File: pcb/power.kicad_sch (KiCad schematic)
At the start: 13 parts, among them J5 12V INPUT 5.08mm >=10A, Q1 FQP47P06 reverse-polarity, U4 AP63205WU-7 fixed 5V

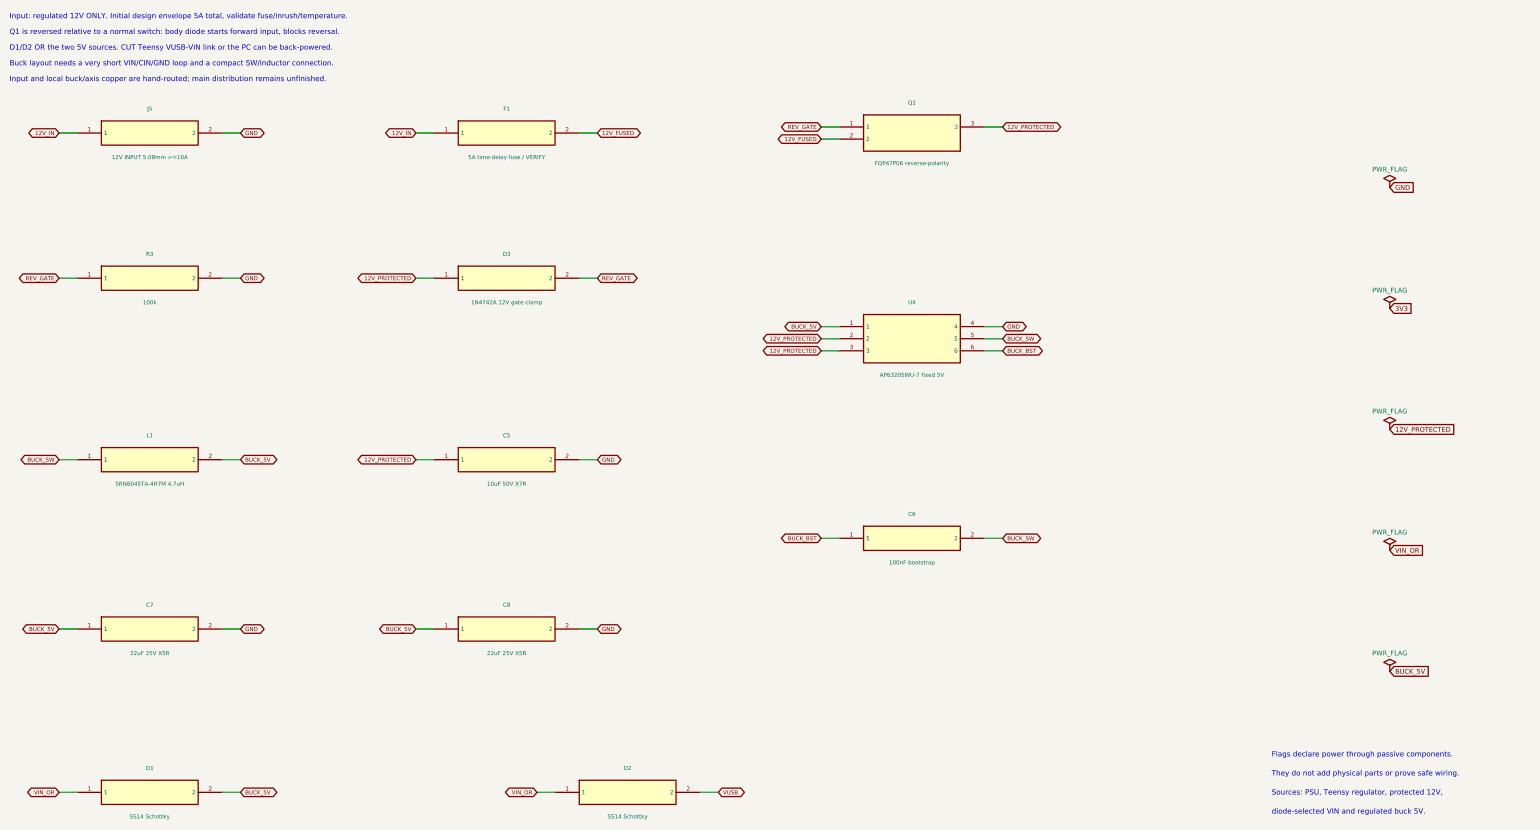
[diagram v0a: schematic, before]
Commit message: feat: finish through-hole six-axis carrier review design
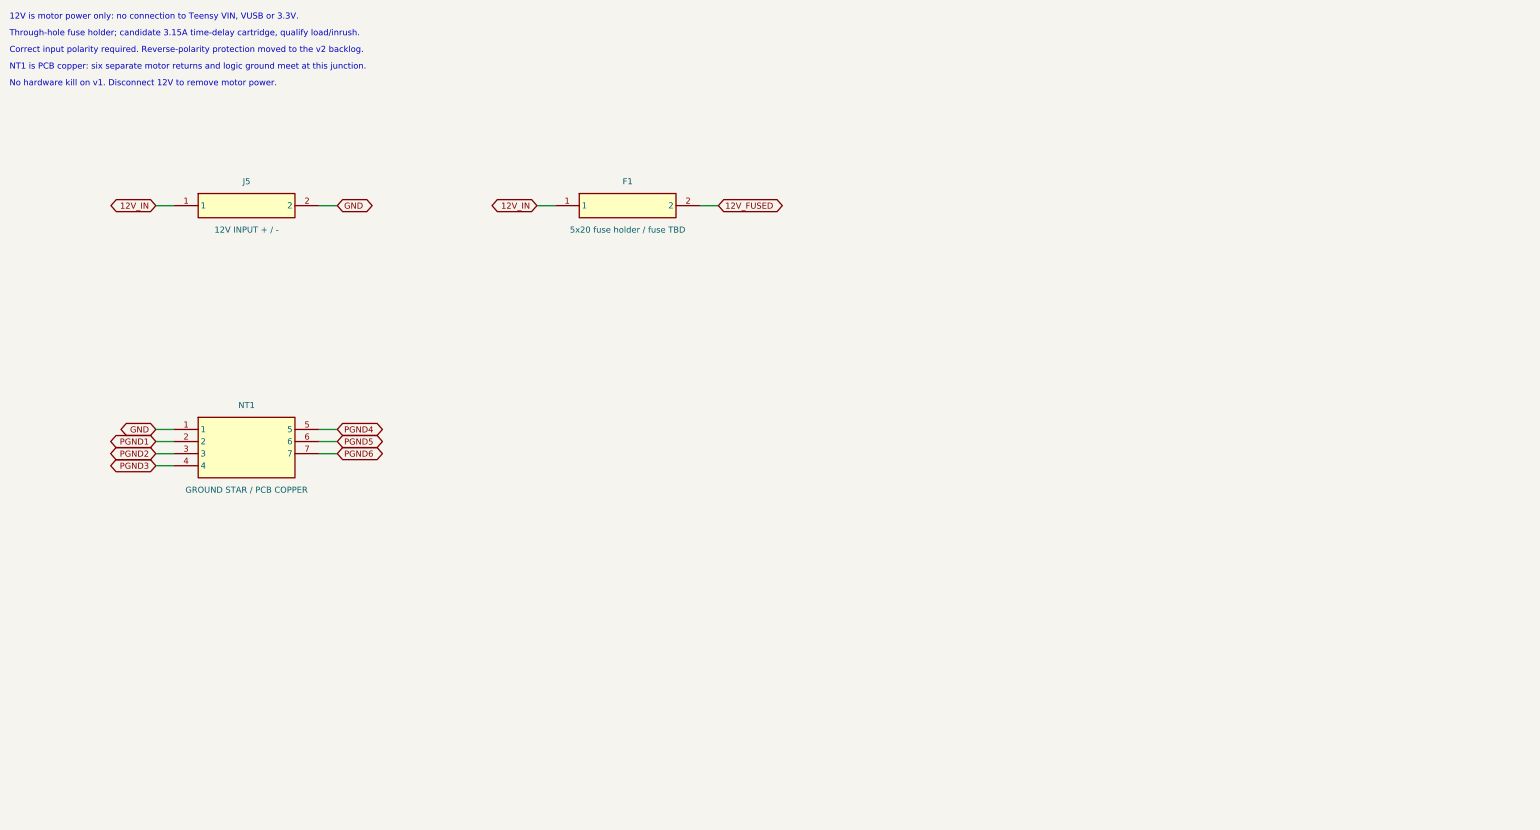
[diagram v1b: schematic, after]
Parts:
- removed C5: 10uF 50V X7R, Capacitor_SMD:C_1210_3225Metric, symbol TrueSkate:C5
- removed C6: 100nF bootstrap, Capacitor_SMD:C_0603_1608Metric, symbol TrueSkate:C6
- removed C7: 22uF 25V X5R, Capacitor_SMD:C_1206_3216Metric, symbol TrueSkate:C7
- removed C8: 22uF 25V X5R, Capacitor_SMD:C_1206_3216Metric, symbol TrueSkate:C8
- removed D1: SS14 Schottky, Diode_SMD:D_SMA, symbol TrueSkate:D1
- removed D2: SS14 Schottky, Diode_SMD:D_SMA, symbol TrueSkate:D2
- removed D3: 1N4742A 12V gate clamp, Diode_THT:D_DO-41_SOD81_P10.16mm_Horizontal, symbol TrueSkate:D3
- removed L1: SRN6045TA-4R7M 4.7uH, Inductor_SMD:L_Bourns_SRN6045TA, symbol TrueSkate:L1
- removed Q1: FQP47P06 reverse-polarity, Package_TO_SOT_THT:TO-220-3_Vertical, symbol TrueSkate:Q1
- removed R3: 100k, Resistor_SMD:R_0603_1608Metric, symbol TrueSkate:R3
- removed U4: AP63205WU-7 fixed 5V, Package_TO_SOT_SMD:TSOT-23-6, symbol TrueSkate:U4
- added NT1: GROUND STAR / PCB COPPER, TrueSkate:GroundStar, symbol TrueSkate:NT1
- F1: value 5A time-delay fuse / VERIFY -> 5x20 fuse holder / fuse TBD
- J5: value 12V INPUT 5.08mm >=10A -> 12V INPUT + / -
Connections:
- net GND: now also NT1.1
- new net PGND1: NT1.2
- new net PGND2: NT1.3
- new net PGND3: NT1.4
- new net PGND4: NT1.5
- new net PGND5: NT1.6
- new net PGND6: NT1.7
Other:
- note added: "12V is motor power only: no connection to Teensy VIN, VUSB or 3.3V."
- note added: "Correct input polarity required. Reverse-polarity protection moved to the v2 backlog."
- note added: "NT1 is PCB copper: six separate motor returns and logic ground meet at this junction."
- note added: "No hardware kill on v1. Disconnect 12V to remove motor power."
- note added: "Through-hole fuse holder; candidate 3.15A time-delay cartridge, qualify load/inrush."
- note removed: "Buck layout needs a very short VIN/CIN/GND loop and a compact SW/inductor connection."
- note removed: "D1/D2 OR the two 5V sources. CUT Teensy VUSB-VIN link or the PC can be back-powered."
- note removed: "Flags declare power through passive components."
- note removed: "Input and local buck/axis copper are hand-routed; main distribution remains unfinished."
- note removed: "Input: regulated 12V ONLY. Initial design envelope 5A total, validate fuse/inrush/temperature."
- note removed: "Q1 is reversed relative to a normal switch: body diode starts forward input, blocks reversal."
- note removed: "Sources: PSU, Teensy regulator, protected 12V,"
- note removed: "They do not add physical parts or prove safe wiring."
- note removed: "diode-selected VIN and regulated buck 5V."
- title: 09 / Power entry and 5V supply -> 08 / Fused 12V and ground star
- moved on the sheet: F1, J5

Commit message: feat: relayout carrier with edge connectors and hardware kill
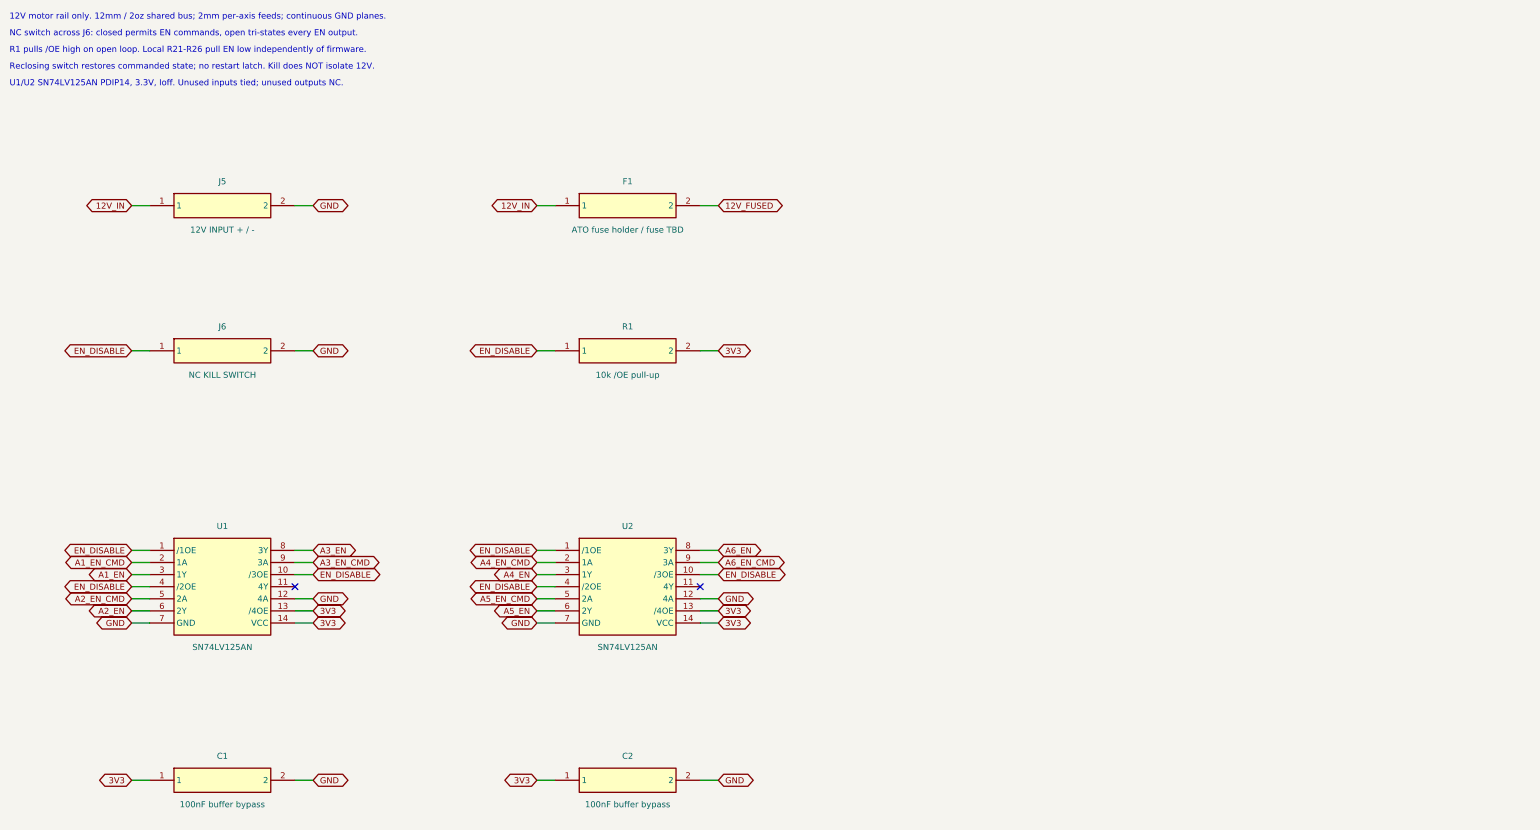
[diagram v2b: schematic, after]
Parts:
- removed NT1: GROUND STAR / PCB COPPER, TrueSkate:GroundStar, symbol TrueSkate:NT1
- added C1: 100nF buffer bypass, TrueSkate:Edge_C_Disc_D5.0mm_W2.5mm_P5.00mm, symbol TrueSkate:C1
- added C2: 100nF buffer bypass, TrueSkate:Edge_C_Disc_D5.0mm_W2.5mm_P5.00mm, symbol TrueSkate:C2
- added J6: NC KILL SWITCH, TrueSkate:Edge_PinHeader_1x02_P2.54mm_Vertical, symbol TrueSkate:J6
- added R1: 10k /OE pull-up, TrueSkate:Edge_R_Axial_DIN0207_L6.3mm_D2.5mm_P7.62mm_Horizontal, symbol TrueSkate:R1
- added U1: SN74LV125AN, TrueSkate:Edge_DIP-14_W7.62mm, symbol TrueSkate:U1
- added U2: SN74LV125AN, TrueSkate:Edge_DIP-14_W7.62mm, symbol TrueSkate:U2
- F1: value 5x20 fuse holder / fuse TBD -> ATO fuse holder / fuse TBD; footprint Fuse:Fuseholder_Cylinder-5x20mm_Schurter_0031_8201_Horizontal_Open -> TrueSkate:Edge_FuseHolder_Blade_ATO_Littelfuse_FLR_178.6165
- J5: footprint TerminalBlock_Phoenix:TerminalBlock_Phoenix_MKDS-1,5-2-5.08_1x02_P5.08mm_Horizontal -> TrueSkate:Edge_TerminalBlock_Phoenix_MKDS-1,5-2-5.08_1x02_P5.08mm_Horizontal
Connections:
- net GND: now also C1.2, C2.2, J6.2, U1.12 (4A), U1.7 (GND), U2.12 (4A), U2.7 (GND)
- new net 3V3: C1.1, C2.1, R1.2, U1.13 (/4OE), U1.14 (VCC), U2.13 (/4OE), U2.14 (VCC)
- new net A1_EN: U1.3 (1Y)
- new net A1_EN_CMD: U1.2 (1A)
- new net A2_EN: U1.6 (2Y)
- new net A2_EN_CMD: U1.5 (2A)
- new net A3_EN: U1.8 (3Y)
- new net A3_EN_CMD: U1.9 (3A)
- new net A4_EN: U2.3 (1Y)
- new net A4_EN_CMD: U2.2 (1A)
- new net A5_EN: U2.6 (2Y)
- new net A5_EN_CMD: U2.5 (2A)
- new net A6_EN: U2.8 (3Y)
- new net A6_EN_CMD: U2.9 (3A)
- new net EN_DISABLE: J6.1, R1.1, U1.1 (/1OE), U1.10 (/3OE), U1.4 (/2OE), U2.1 (/1OE), U2.10 (/3OE), U2.4 (/2OE)
- no-connect marks 0 -> 2
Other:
- note added: "12V motor rail only. 12mm / 2oz shared bus; 2mm per-axis feeds; continuous GND planes."
- note added: "NC switch across J6: closed permits EN commands, open tri-states every EN output."
- note added: "R1 pulls /OE high on open loop. Local R21-R26 pull EN low independently of firmware."
- note added: "Reclosing switch restores commanded state; no restart latch. Kill does NOT isolate 12V."
- note added: "U1/U2 SN74LV125AN PDIP14, 3.3V, Ioff. Unused inputs tied; unused outputs NC."
- note removed: "12V is motor power only: no connection to Teensy VIN, VUSB or 3.3V."
- note removed: "Correct input polarity required. Reverse-polarity protection moved to the v2 backlog."
- note removed: "NT1 is PCB copper: six separate motor returns and logic ground meet at this junction."
- note removed: "No hardware kill on v1. Disconnect 12V to remove motor power."
- note removed: "Through-hole fuse holder; candidate 3.15A time-delay cartridge, qualify load/inrush."
- title: 08 / Fused 12V and ground star -> 08 / Power and hardware kill
- moved on the sheet: J5

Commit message: fix: refine carrier clearances and routing with populated renders
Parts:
- F1: value ATO fuse holder / fuse TBD -> Keystone 3557-2 ATO holder; footprint TrueSkate:Edge_FuseHolder_Blade_ATO_Littelfuse_FLR_178.6165 -> TrueSkate:Keystone_3557-2_ATO
